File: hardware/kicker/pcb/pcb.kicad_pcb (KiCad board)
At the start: 2 copper layers, 108.7 x 42.8 mm, 35 parts, among them J1 Conn_01x04, J2 Conn_01x04, J3 Conn_01x02, Q1 NMOS, U1 XL6019E1, U2 TS4535TP 250GF 009, U4 TC4427AEOA713_C5804606

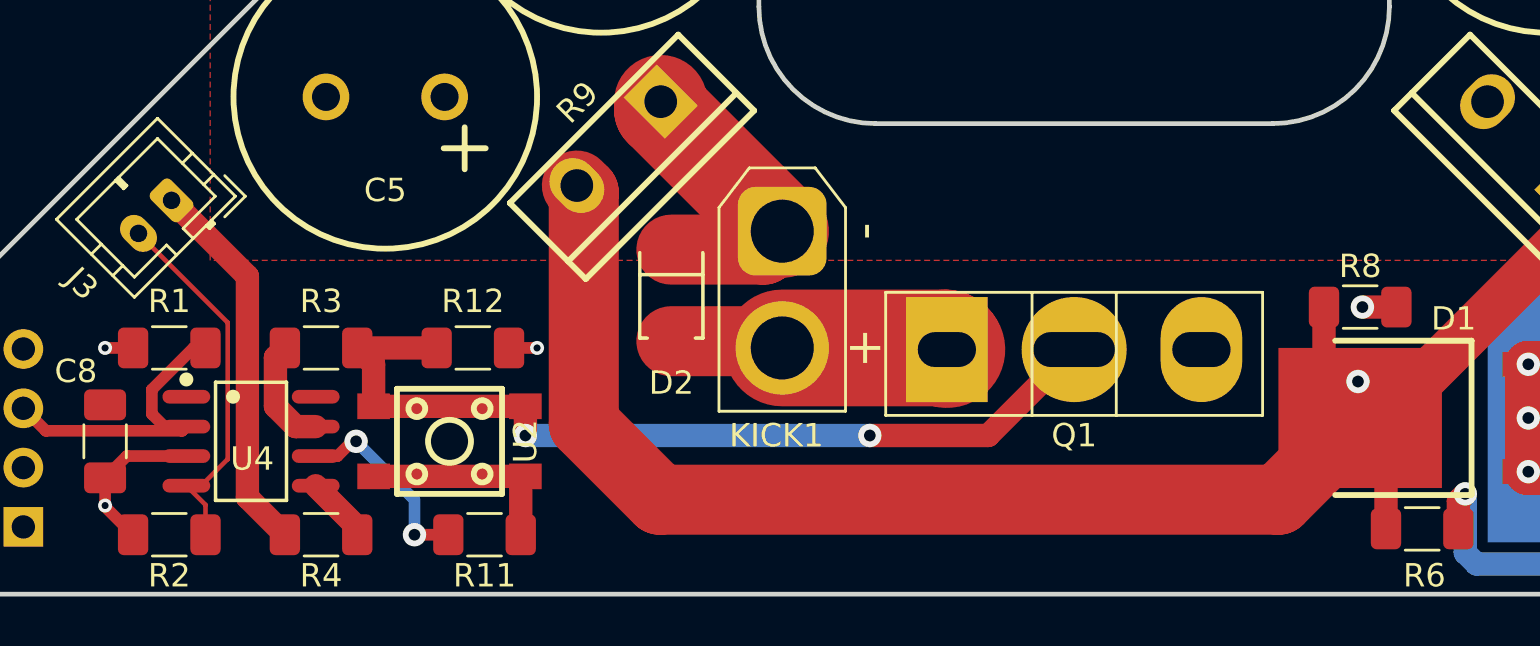
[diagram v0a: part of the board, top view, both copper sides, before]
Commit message: fixed motor driver footprint (one header had markings on bottom surface for some reason), generated production files
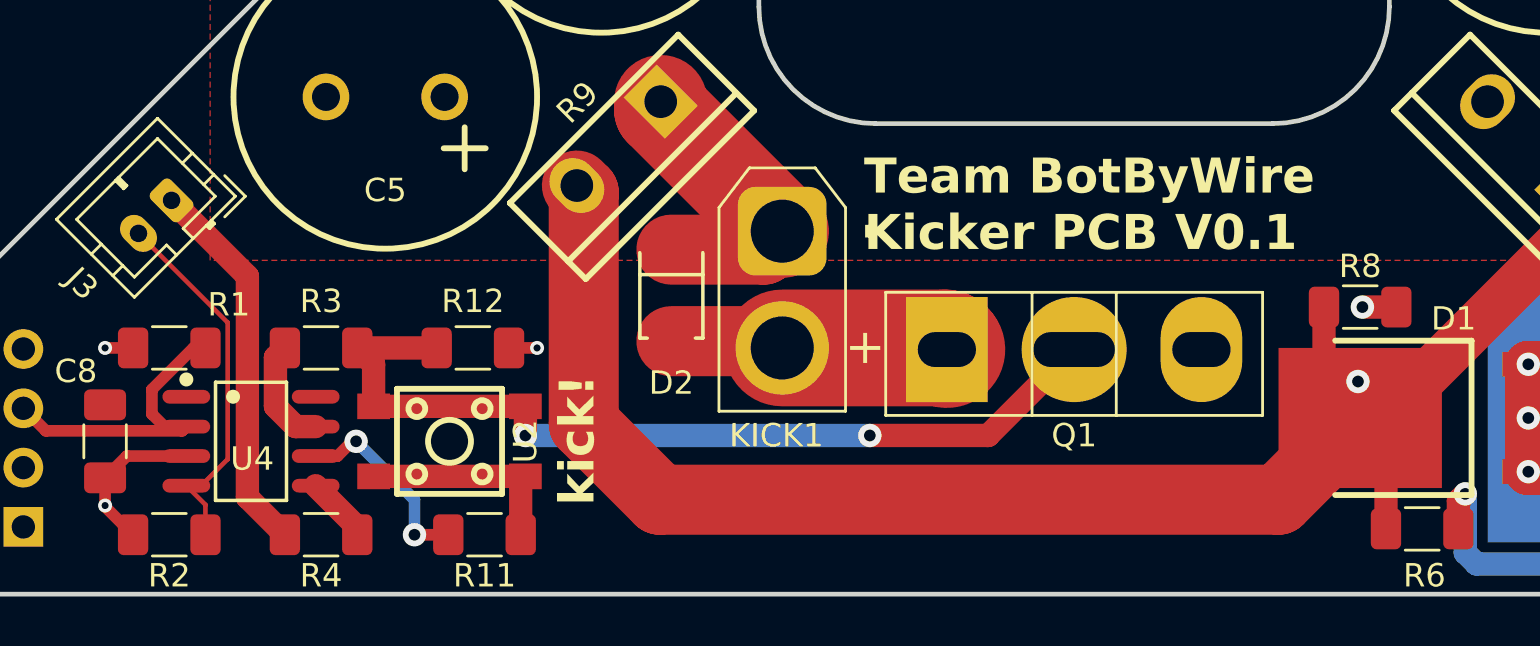
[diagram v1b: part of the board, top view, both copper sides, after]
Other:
- board text added: "Team BotByWire Kicker PCB V0.1"
- board text added: "kick!"
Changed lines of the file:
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@@
 		(tags "resistor handsolder")
 		(property "Reference" "R1"
-			(at 0 -2 180)
+			(at 2.55 -1.855 0)
 			(layer "F.SilkS")
 			(effects
@@
 		(layer "Edge.Cuts")
 	)
-	(gr_text_box "VCC | INA | GND | GND"
-		(start -47.6 -1.295)
-		(end -46.2 -11.545)
+	(gr_text "Team BotByWire\nKicker PCB V0.1"
+		(at -9 -14.6 0)
+		(layer "F.SilkS")
+		(effects
+			(font
+				(size 1.5 1.5)
+				(thickness 0.3)
+				(bold yes)
+			)
+			(justify left bottom)
+		)
+	)
+	(gr_text "kick!"
+		(at -20.4 -3.8 90)
+		(layer "F.SilkS")
+		(effects
+			(font
+				(size 1.5 1.5)
+				(thickness 0.3)
+				(bold yes)
+			)
+			(justify left bottom)
+		)
+	)
+	(gr_text_box "VCC|INA|GND|GND"
+		(start -48 -1.475)
+		(end -46.6 -11.725)
 		(angle 90)
 		(layer "F.SilkS")
 		(effects
 			(font
-				(size 0.5 0.5)
-				(thickness 0.1)
+				(size 0.8 0.8)
+				(thickness 0.15)
 				(bold yes)
 			)
@@
 	(gr_text_box "INB|OUTB"
 		(pts
-			(xy -38.80023 -13.94977) (xy -35.971803 -16.778197) (xy -34.981853 -15.788248) (xy -37.810281 -12.959821)
+			(xy -39.215179 -13.564719) (xy -36.386752 -16.393146) (xy -35.396802 -15.403197) (xy -38.22523 -12.57477)
 		)
 		(angle 45)
@@
 		(effects
 			(font
-				(size 0.5 0.5)
-				(thickness 0.1)
+				(size 0.8 0.8)
+				(thickness 0.15)
 				(bold yes)
 			)
@@
 		)
 	)
-	(gr_text_box "GND | GND | VCC | VCC"
-		(start 46.1 -1.15)
-		(end 47.5 -11.65)
+	(gr_text_box "GND|GND|VCC|VCC"
+		(start 45.8 0.05)
+		(end 47.2 -10.45)
 		(angle 90)
 		(layer "F.SilkS")
 		(effects
 			(font
-				(size 0.5 0.5)
-				(thickness 0.1)
+				(size 0.8 0.8)
+				(thickness 0.15)
 				(bold yes)
 			)
